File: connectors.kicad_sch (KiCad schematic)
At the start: 34 parts, among them J10 1755736, J11 USB_C_Receptacle_USB2.0_16P, J12 1755736, J13 1755736, J14 Conn_02x06_Odd_Even, J15 1755736, J16 1755736, J17 Conn_02x06_Odd_Even, J18 1755736, J19 1755736, J20 Conn_02x06_Odd_Even, J21 1755736, J22 1755736, Q7 STL40DN3LLH5, U3 INA236BIDDFR, U4 INA236AIDDFR, U5 INA236AIDDFR, U6 INA236AIDDFR, U9 TCPP02-M18

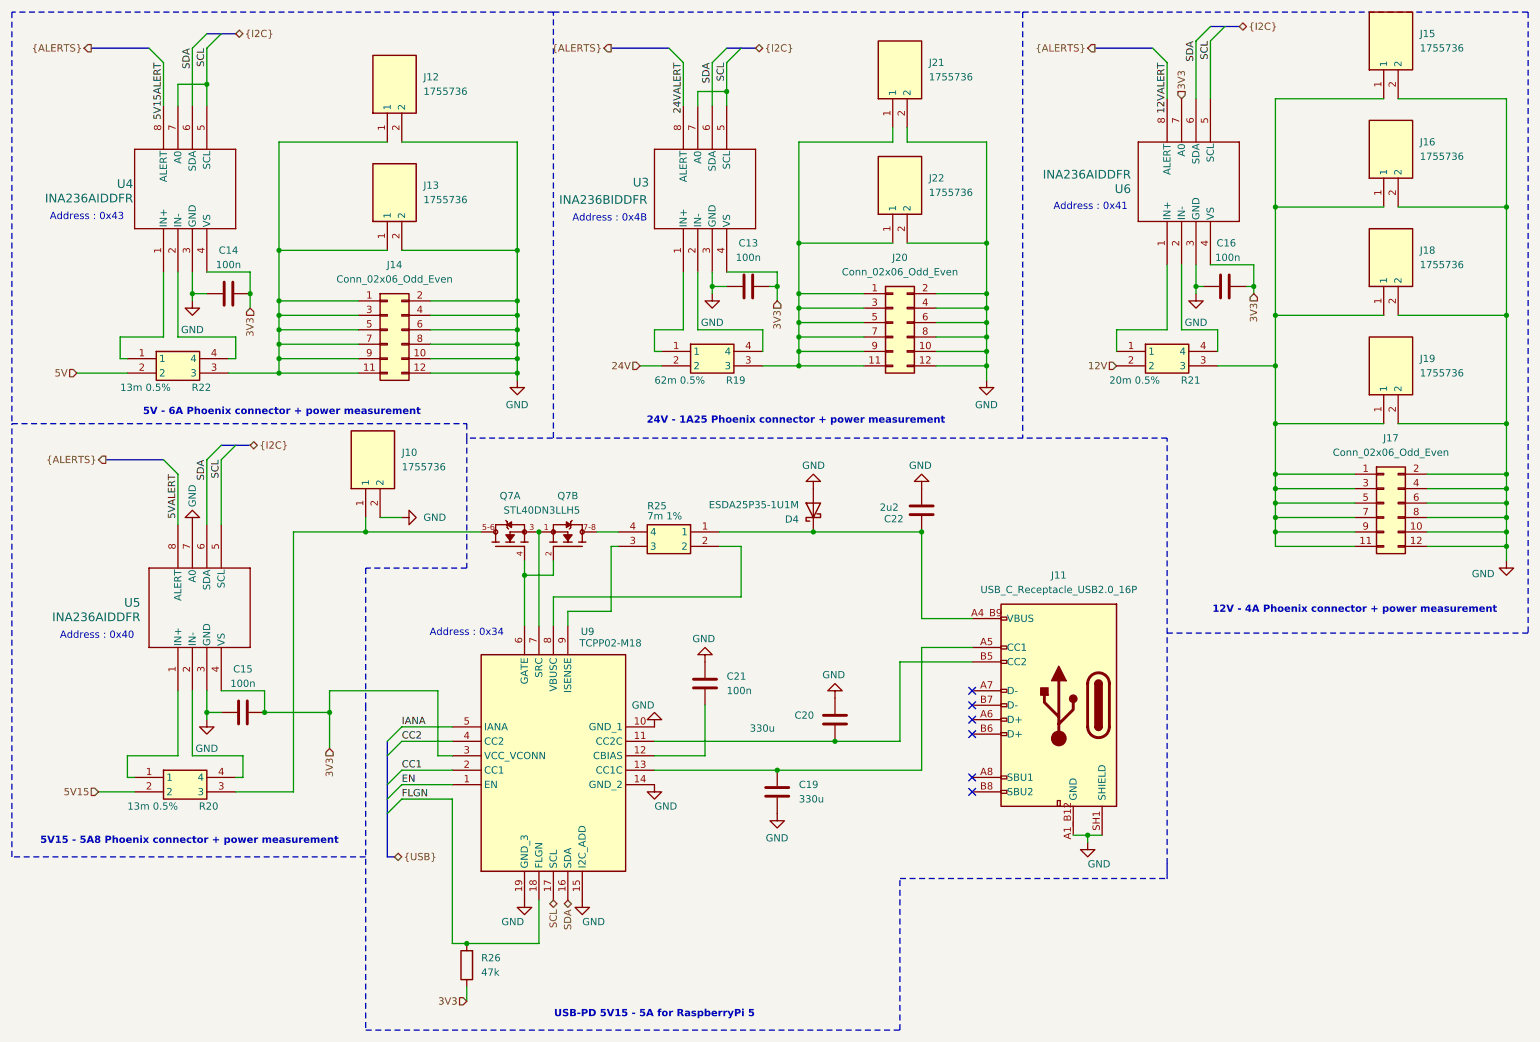
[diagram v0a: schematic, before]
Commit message: Correctifs et améliorations + passage à KiCad V9
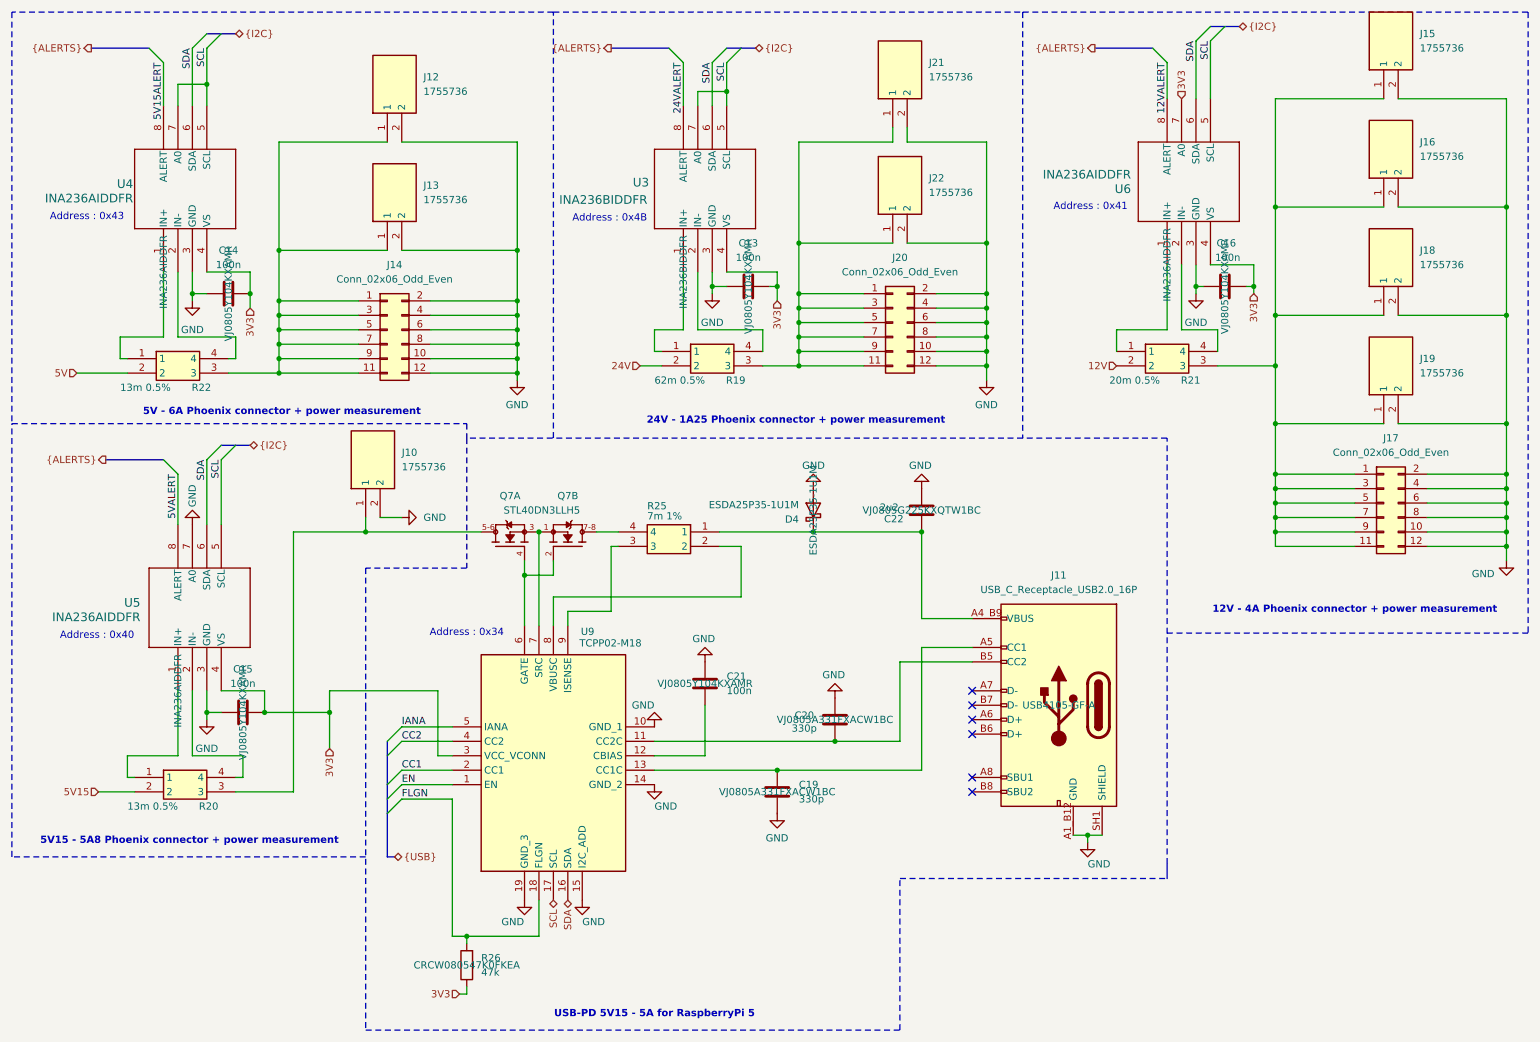
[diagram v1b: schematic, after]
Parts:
- C13, C14, C15, C16, C21: Manufacturer_Part_Number (none) -> VJ0805Y104KXAMR
- C19, C20: value 330u -> 330p; Manufacturer_Part_Number (none) -> VJ0805A331FXACW1BC
- C22: Manufacturer_Part_Number (none) -> VJ0805G225KXQTW1BC
- D4: Manufacturer_Part_Number (none) -> ESDA25P35-1U1M
- J11: Manufacturer_Part_Number (none) -> USB4105-GF-A
- R19: Manufacturer_Part_Number L4CL1206LR013DNR -> L4CL1206LR062DNR
- R21: Manufacturer_Part_Number L4CL1206LR013DNR -> L4CL1206LR020DNR
- R25: Manufacturer_Part_Number L4CL1206LR013DNR -> L4CL1206LR007FNR
- R26: Manufacturer_Part_Number (none) -> CRCW080547K0FKEA
- U3: Manufacturer_Part_Number (none) -> INA236BIDDFR
- U4, U5, U6: Manufacturer_Part_Number (none) -> INA236AIDDFR
- U9: Manufacturer_Part_Number TCPP02-M18 -> (none)
